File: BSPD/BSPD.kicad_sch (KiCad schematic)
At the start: 40 parts, among them J1 DT13-48PABCD-R015, K1 Latching Relay, Q1 STS6NF20V, Q2 STS6NF20V, Q3 STS6NF20V, U1 LM7805CT, U10 DK1A1B-12V, U12 LM555N, U13 LM7805CT, U2 NSL-32, U2 OP AMP, U3 OP AMP, U5 2x4 OR GATE, U6 LM555N, U8 NAND, U9 AND GATE

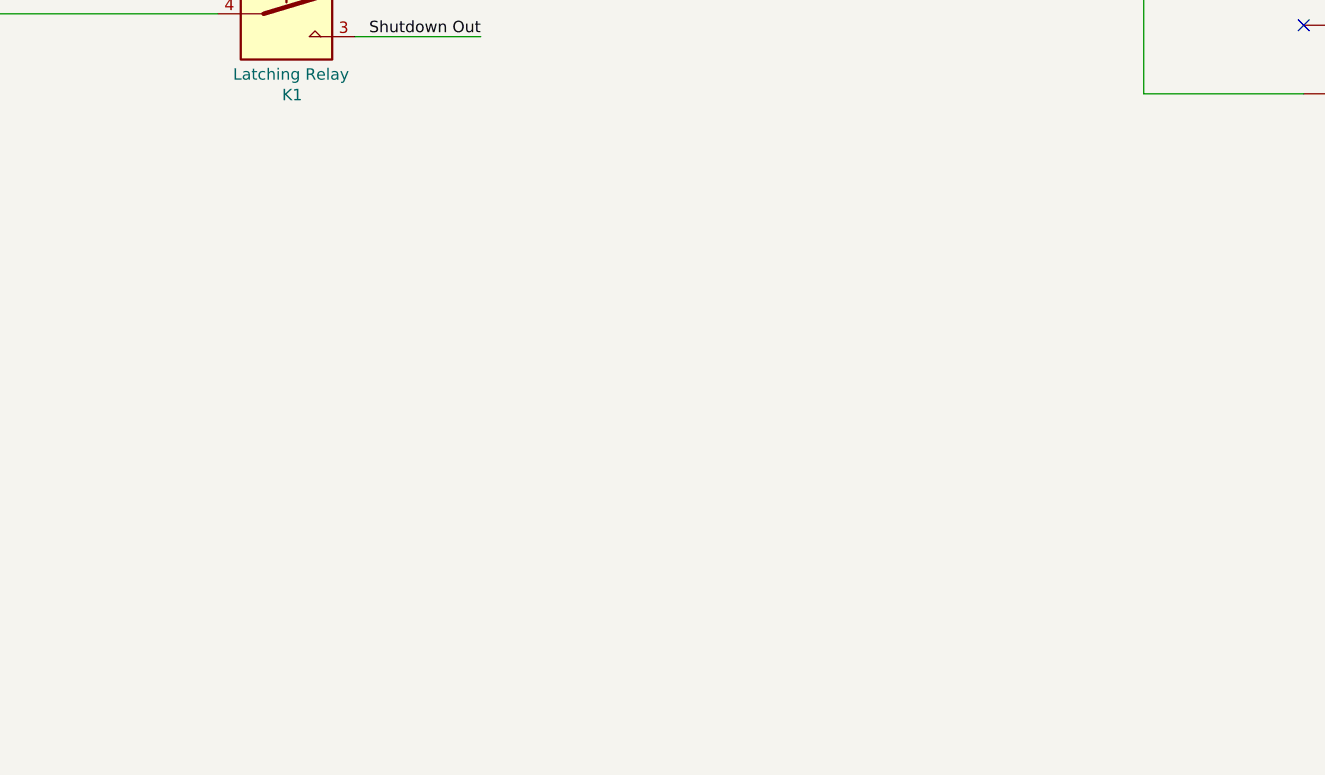
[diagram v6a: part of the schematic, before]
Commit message: Added micro and CAN
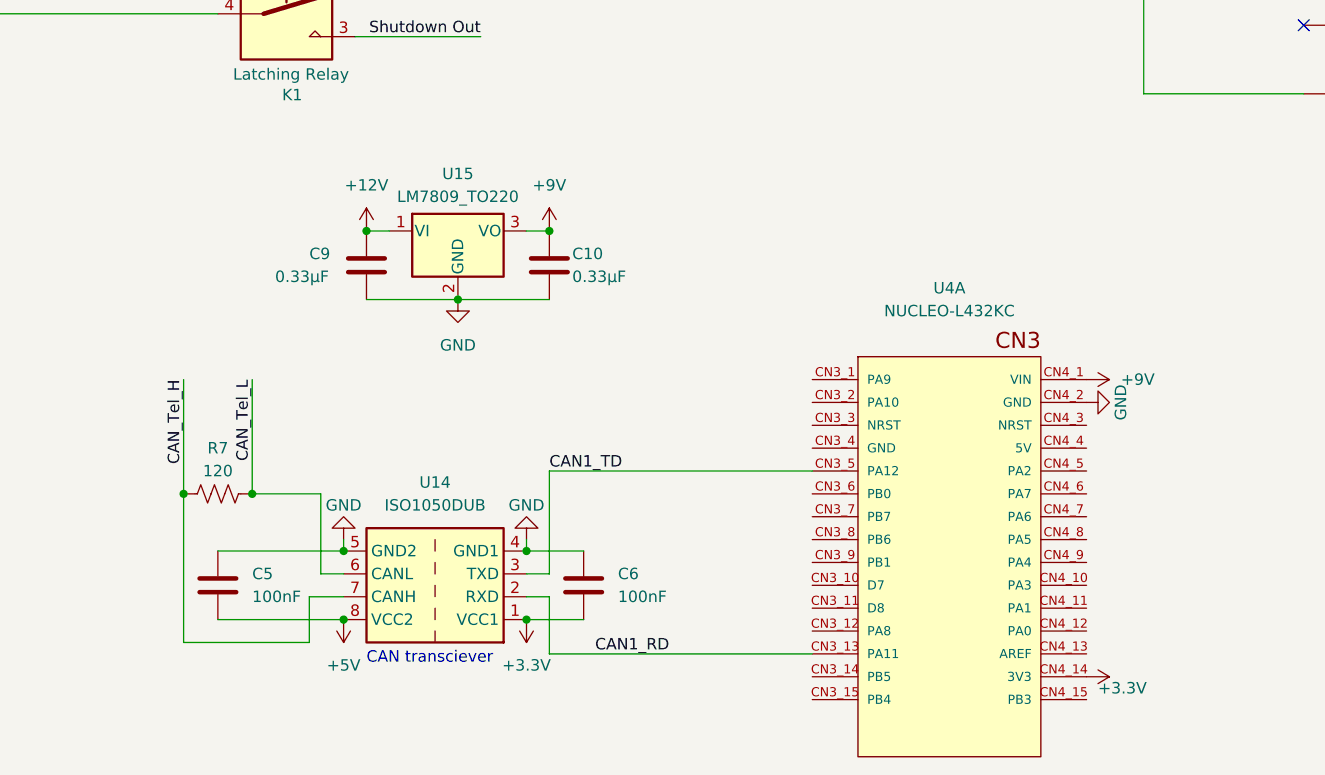
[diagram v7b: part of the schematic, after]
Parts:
- added C10, C9: 0.33µF, Capacitor_SMD:C_0805_2012Metric_Pad1.18x1.45mm_HandSolder, symbol Device:C
- added C5, C6: 100nF, Capacitor_SMD:C_0805_2012Metric_Pad1.18x1.45mm_HandSolder, symbol Device:C
- added R7: 120, Resistor_SMD:R_0805_2012Metric_Pad1.20x1.40mm_HandSolder, symbol Device:R_US
- added U14: ISO1050DUB, Package_SO:SOP-8_6.62x9.15mm_P2.54mm, symbol Interface_CAN_LIN:ISO1050DUB
- added U15: LM7809_TO220, Package_TO_SOT_THT:TO-220-3_Vertical, symbol Regulator_Linear:LM7809_TO220
- added U4: NUCLEO-L432KC, 1FS_2_Global_Footprint_Library:MODULE_NUCLEO-L432KC, symbol 1_ACC_BOARD:NUCLEO-L432KC
- U1, U13: footprint 1FS_2_Global_Footprint_Library:Basic 3 Hole -> Package_TO_SOT_THT:TO-220-3_Vertical
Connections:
- net +12V: now also C9.1, U15.1 (VI)
- net +5V: now also C5.2, U14.8 (VCC2)
- net GND: now also C10.2, C5.1, C6.1, C9.2, U14.4 (GND1), U14.5 (GND2), U15.2 (GND), U4.CN4_2 (GND)
- new net +3.3V: C6.2, U14.1 (VCC1), U4.CN4_14 (3V3)
- new net +9V: C10.1, U15.3 (VO), U4.CN4_1 (VIN)
- new net CAN1_RD: U14.2 (RXD), U4.CN3_13 (PA11)
- new net CAN1_TD: U14.3 (TXD), U4.CN3_5 (PA12)
- new net CAN_Tel_H: R7.2, U14.7 (CANH)
- new net CAN_Tel_L: R7.1, U14.6 (CANL)
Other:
- note added: "CAN transciever"

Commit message: Acc BSPD Split again
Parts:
- removed Q1: STS6NF20V, 1FS_2_Global_Footprint_Library:SO-8_STM, symbol 1_ACC_BOARD:STS6NF20V
- removed unit 1 of U8
- added C11, C12, C13, C14, C15, C16, C17: 100nf, Capacitor_SMD:C_0805_2012Metric_Pad1.18x1.45mm_HandSolder, symbol Device:C
- added D4, D5: D, Diode_SMD:D_2010_5025Metric_Pad1.52x2.65mm_HandSolder, symbol Device:D
- added K2: Latching Relay, 1FS_2_Global_Footprint_Library:Omron G6BK-1114P-US, symbol 1_Personal_FS_Library:G6BK-1114P-US
- added Q4: STS6NF20V, 1FS_2_Global_Footprint_Library:SO-8_STM, symbol 1_ACC_BOARD:STS6NF20V
- added R13: 374, Resistor_SMD:R_0805_2012Metric_Pad1.20x1.40mm_HandSolder, symbol Device:R_US
- added U17: NAND, Package_DIP:DIP-14_W7.62mm, symbol 4xxx:4023
- added U?: NSL-32, 1FS_2_Global_Footprint_Library:OptoCoupler 6-SOP, symbol Isolator:NSL-32
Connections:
- net +12V: now also U?.4 (R)
- net +5V: now also U6.8 (VCC), C11.2, C12.2, C13.2, C14.2, C15.2, C16.2, C17.2, U17.14 (VDD)
- net 3V: no longer U3.9
- net BMS_FAULT 5V: now also J1.A10, U17.8; no longer U3.8
- net BSPD Fault: now also U8.9; no longer U8.6
- net BSPD_FAULT: now also U?.1 (A)
- net Brake Output: now also U2.5
- net CAN_Tel_H: now also J1.B1
- net CAN_Tel_L: now also J1.B2
- net Current Output: no longer U2.5
- net GND: now also D1.2 (A), K1.2, C11.1, C12.1, C13.1, C14.1, C15.1, C16.1, C17.1, D5.2 (A), K2.1, Q4.1 (S), Q4.2 (S), Q4.3 (S), R13.1, U17.7 (VSS)
- net IMD Latch Delay: now also Q4.4 (G)
- net IMD_FAULT: no longer J1.A9
- net IMD_FAULT 5V: now also J1.A9, U17.1, U17.2
- net SH_RESET: now also D5.1 (K), K2.6
- net Shutdown Out: now also K2.3
- net at C3.1, U5.13, U6.4 (R): no longer U6.8 (VCC)
- net 4.1V renamed Brake Threshhold (4.1V)
- net BMS_FAULT 3.3V: no longer names the net of U3.10
- net BMS_FAULT 3.3V: no longer J1.A10
- new net: U6.3 (Q), U8.1, U8.2, U8.8
- new net: U17.9, U?.1 (A)
- new net: D4.2 (A), K2.2, Q4.5 (D), Q4.6 (D), Q4.7 (D), Q4.8 (D)
- new net: D4.1 (K), K2.5, U?.3 (R)
- new net: R13.2, U?.2 (K)
- no-connect marks 45 -> 46
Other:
- moved on the sheet: C4, C7, C8, R17, U12, U13
